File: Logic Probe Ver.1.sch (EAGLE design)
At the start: 48 parts, among them J5 TST-125-01-G-D, U1 DS90LV047ATM, U2 DS90LV047ATM, U3 DS90LV047ATM, U4 DS90LV047ATM, U5 SN74BCT543DW, U6 SN74BCT543DW

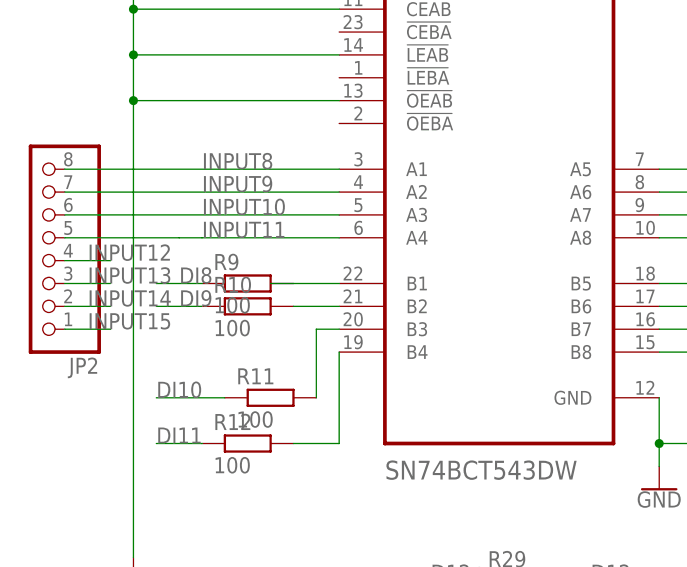
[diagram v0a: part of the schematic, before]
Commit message: PCB Submission
Attempt to fix the comments received for PCB
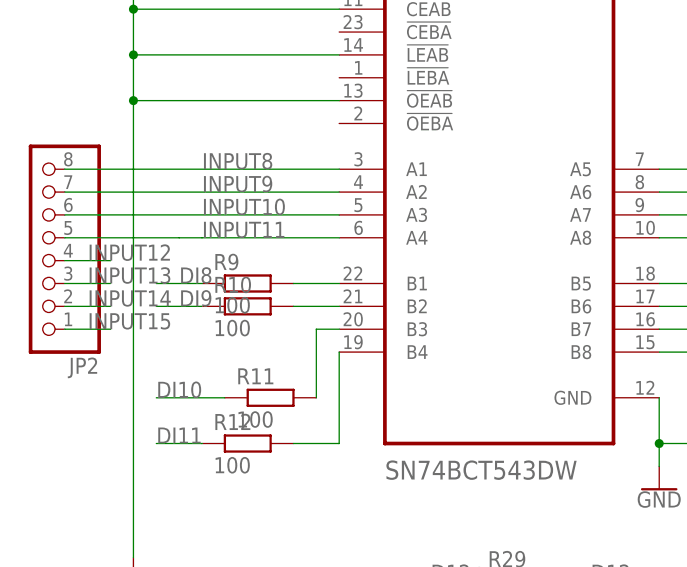
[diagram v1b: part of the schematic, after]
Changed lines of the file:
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@@
-</segment>
-</net>
-<net name="N$4" class="0">
-<segment>
-<pinref part="R9" gate="G$1" pin="2"/>
-<wire x1="-5.08" y1="17.78" x2="-7.62" y2="17.78" width="0.1524" layer="91"/>
-<wire x1="-5.08" y1="17.78" x2="0" y2="17.78" width="0.1524" layer="91"/>
-<pinref part="U6" gate="A" pin="B1"/>
 </segment>
 </net>
@@
 </segment>
 </net>
+<net name="N$4" class="0">
+<segment>
+<pinref part="R9" gate="G$1" pin="2"/>
+<pinref part="U6" gate="A" pin="B1"/>
+<wire x1="-5.08" y1="17.78" x2="0" y2="17.78" width="0.1524" layer="91"/>
+</segment>
+</net>
